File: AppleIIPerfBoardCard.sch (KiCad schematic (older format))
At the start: 2 parts

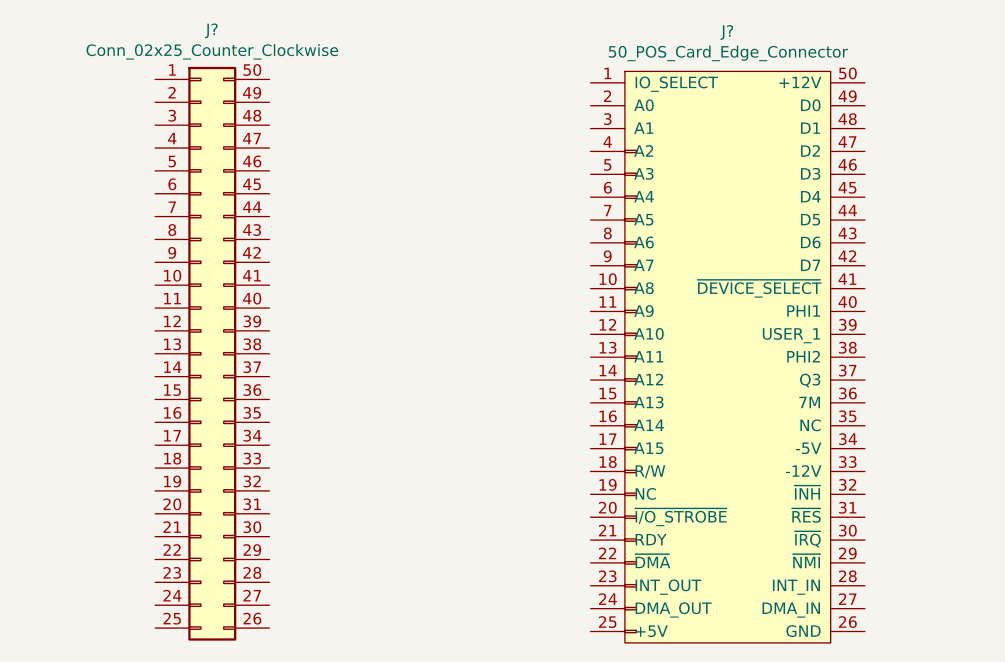
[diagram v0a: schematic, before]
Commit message: added netlist and created main board edge and grid of pads
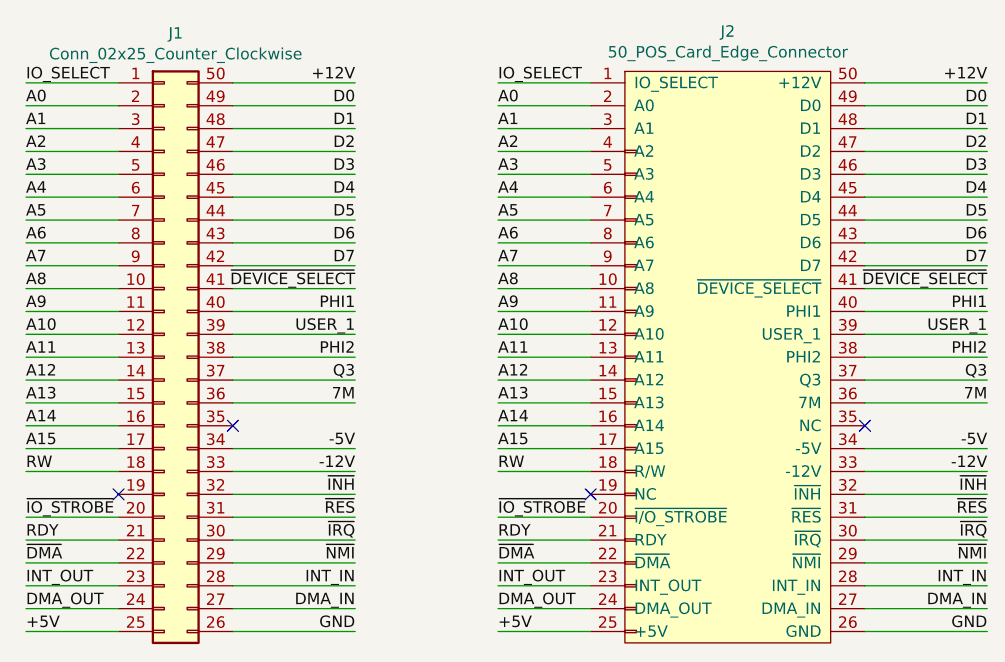
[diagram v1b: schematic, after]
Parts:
- J1: renamed from J?; footprint (none) -> AppleIIPerfBoardCard:2x25_P2.54mm_Vertical
- J2: renamed from J?; footprint (none) -> AppleIIPerfBoardCard:50_POS_CARD_EDGE
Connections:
- net IO_SELECT: now reaches J1.1 (Pin_1)
- net IO_SELECT: now also J2.1 (IO_SELECT)
- net A8: now reaches J1.10 (Pin_10)
- net A8: now also J2.10 (A8)
- net A9: now reaches J1.11 (Pin_11)
- net A9: now also J2.11 (A9)
- net A10: now reaches J1.12 (Pin_12)
- net A10: now also J2.12 (A10)
- net A11: now reaches J1.13 (Pin_13)
- net A11: now also J2.13 (A11)
- net A12: now reaches J1.14 (Pin_14)
- net A12: now also J2.14 (A12)
- net A13: now reaches J1.15 (Pin_15)
- net A13: now also J2.15 (A13)
- net A14: now reaches J1.16 (Pin_16)
- net A14: now also J2.16 (A14)
- net A15: now reaches J1.17 (Pin_17)
- net A15: now also J2.17 (A15)
- net RW: now reaches J1.18 (Pin_18)
- net RW: now also J2.18 (R/W)
- net A0: now reaches J1.2 (Pin_2)
- net A0: now also J2.2 (A0)
- net ~IO_STROBE: now reaches J1.20 (Pin_20)
- net ~IO_STROBE: now also J2.20 (~I/O_STROBE)
- net RDY: now reaches J1.21 (Pin_21)
- net RDY: now also J2.21 (RDY)
- net ~DMA: now reaches J1.22 (Pin_22)
- net ~DMA: now also J2.22 (~DMA)
- net INT_OUT: now reaches J1.23 (Pin_23)
- net INT_OUT: now also J2.23 (INT_OUT)
- net DMA_OUT: now reaches J1.24 (Pin_24)
- net DMA_OUT: now also J2.24 (DMA_OUT)
- net +5V: now reaches J1.25 (Pin_25)
- net +5V: now also J2.25 (+5V)
- net GND: now reaches J1.26 (Pin_26)
- net GND: now also J2.26 (GND)
- net DMA_IN: now reaches J1.27 (Pin_27)
- net DMA_IN: now also J2.27 (DMA_IN)
- net INT_IN: now reaches J1.28 (Pin_28)
- net INT_IN: now also J2.28 (INT_IN)
- net ~NMI: now reaches J1.29 (Pin_29)
- net ~NMI: now also J2.29 (~NMI)
- net A1: now reaches J1.3 (Pin_3)
- net A1: now also J2.3 (A1)
- net ~IRQ: now reaches J1.30 (Pin_30)
- net ~IRQ: now also J2.30 (~IRQ)
- net ~RES: now reaches J1.31 (Pin_31)
- net ~RES: now also J2.31 (~RES)
- net ~INH: now reaches J1.32 (Pin_32)
- net ~INH: now also J2.32 (~INH)
- net -12V: now reaches J1.33 (Pin_33)
- net -12V: now also J2.33 (-12V)
- net -5V: now reaches J1.34 (Pin_34)
- net -5V: now also J2.34 (-5V)
- net 7M: now reaches J1.36 (Pin_36)
- net 7M: now also J2.36 (7M)
- net Q3: now reaches J1.37 (Pin_37)
- net Q3: now also J2.37 (Q3)
- net PHI2: now reaches J1.38 (Pin_38)
- net PHI2: now also J2.38 (PHI2)
- net USER_1: now reaches J1.39 (Pin_39)
- net USER_1: now also J2.39 (USER_1)
- net A2: now reaches J1.4 (Pin_4)
- net A2: now also J2.4 (A2)
- net PHI1: now reaches J1.40 (Pin_40)
- net PHI1: now also J2.40 (PHI1)
- net ~DEVICE_SELECT: now reaches J1.41 (Pin_41)
- net ~DEVICE_SELECT: now also J2.41 (~DEVICE_SELECT)
- net D7: now reaches J1.42 (Pin_42)
- net D7: now also J2.42 (D7)
- net D6: now reaches J1.43 (Pin_43)
- net D6: now also J2.43 (D6)
- net D5: now reaches J1.44 (Pin_44)
- net D5: now also J2.44 (D5)
- net D4: now reaches J1.45 (Pin_45)
- net D4: now also J2.45 (D4)
- net D3: now reaches J1.46 (Pin_46)
- net D3: now also J2.46 (D3)
- net D2: now reaches J1.47 (Pin_47)
- net D2: now also J2.47 (D2)
- net D1: now reaches J1.48 (Pin_48)
- net D1: now also J2.48 (D1)
- net D0: now reaches J1.49 (Pin_49)
- net D0: now also J2.49 (D0)
- net A3: now reaches J1.5 (Pin_5)
- net A3: now also J2.5 (A3)
- net +12V: now reaches J1.50 (Pin_50)
- net +12V: now also J2.50 (+12V)
- net A4: now reaches J1.6 (Pin_6)
- net A4: now also J2.6 (A4)
- net A5: now reaches J1.7 (Pin_7)
- net A5: now also J2.7 (A5)
- net A6: now reaches J1.8 (Pin_8)
- net A6: now also J2.8 (A6)
- net A7: now reaches J1.9 (Pin_9)
- net A7: now also J2.9 (A7)
- no-connect marks 0 -> 4
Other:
- moved on the sheet: J1
